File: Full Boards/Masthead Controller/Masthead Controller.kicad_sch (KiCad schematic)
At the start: 181 parts, among them Q1 2N7002, Q2 2N7002, Q3 BSS138P,215, Q4 BSS138P,215, SW1 SW_MEC_5G, SW2 SW_MEC_5G

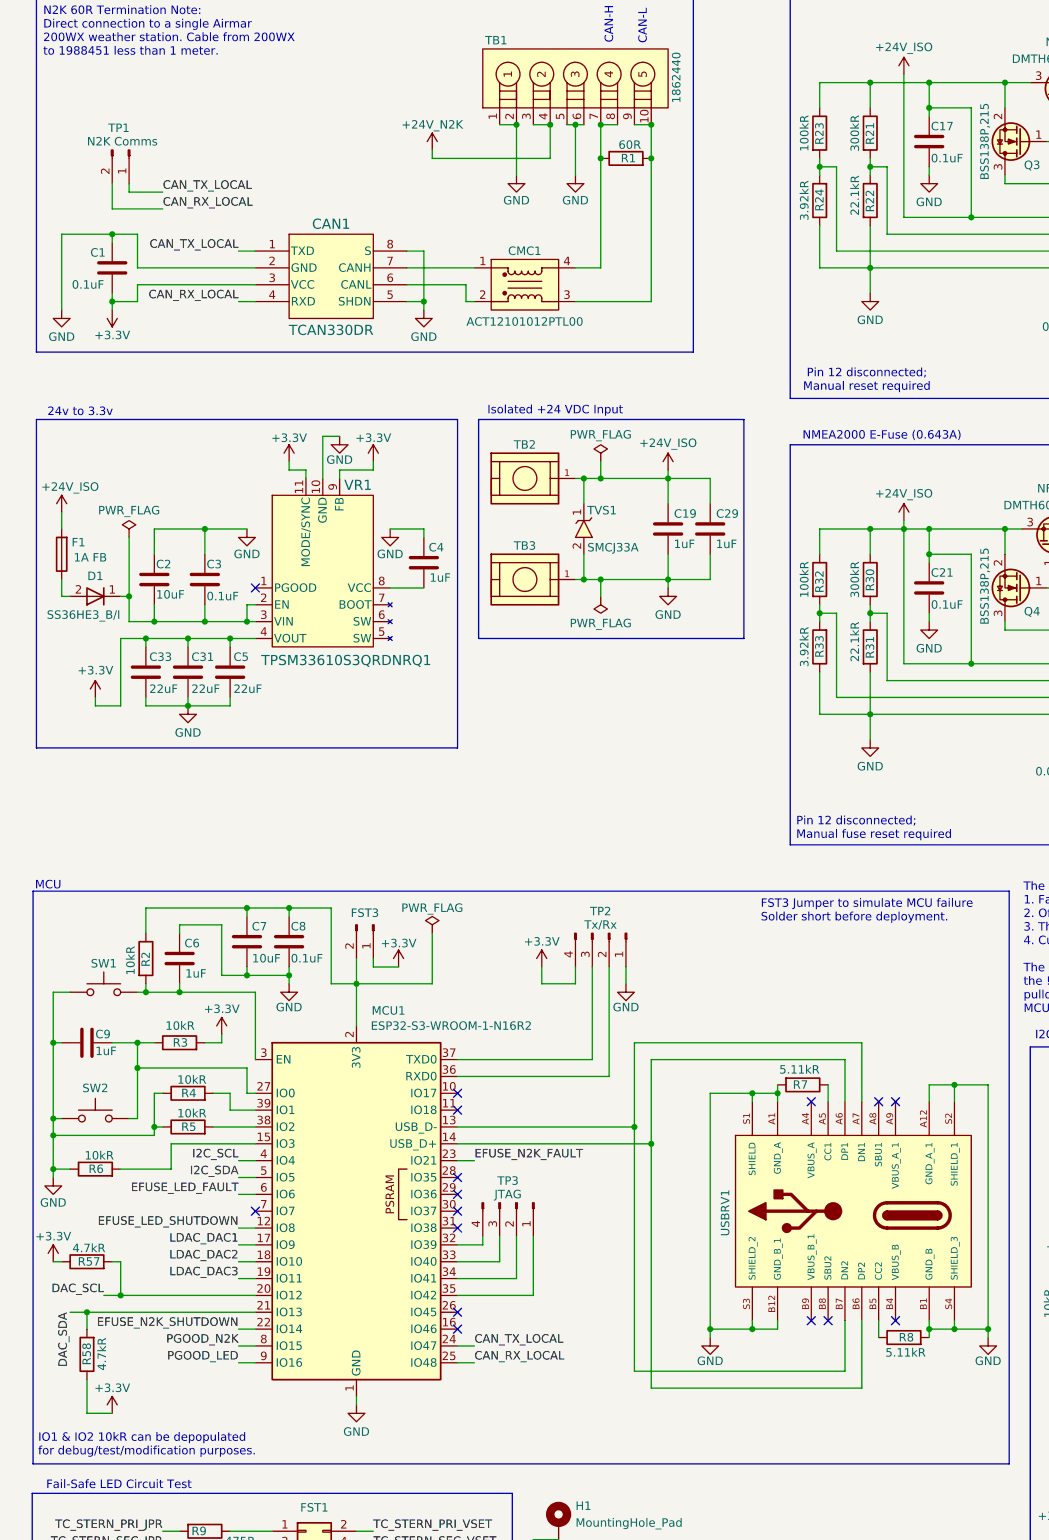
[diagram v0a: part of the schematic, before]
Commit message: Beginning work to enable powering the MCU over USB.
Signed-off-by: digimer <digital.mermaid@gmail.com>
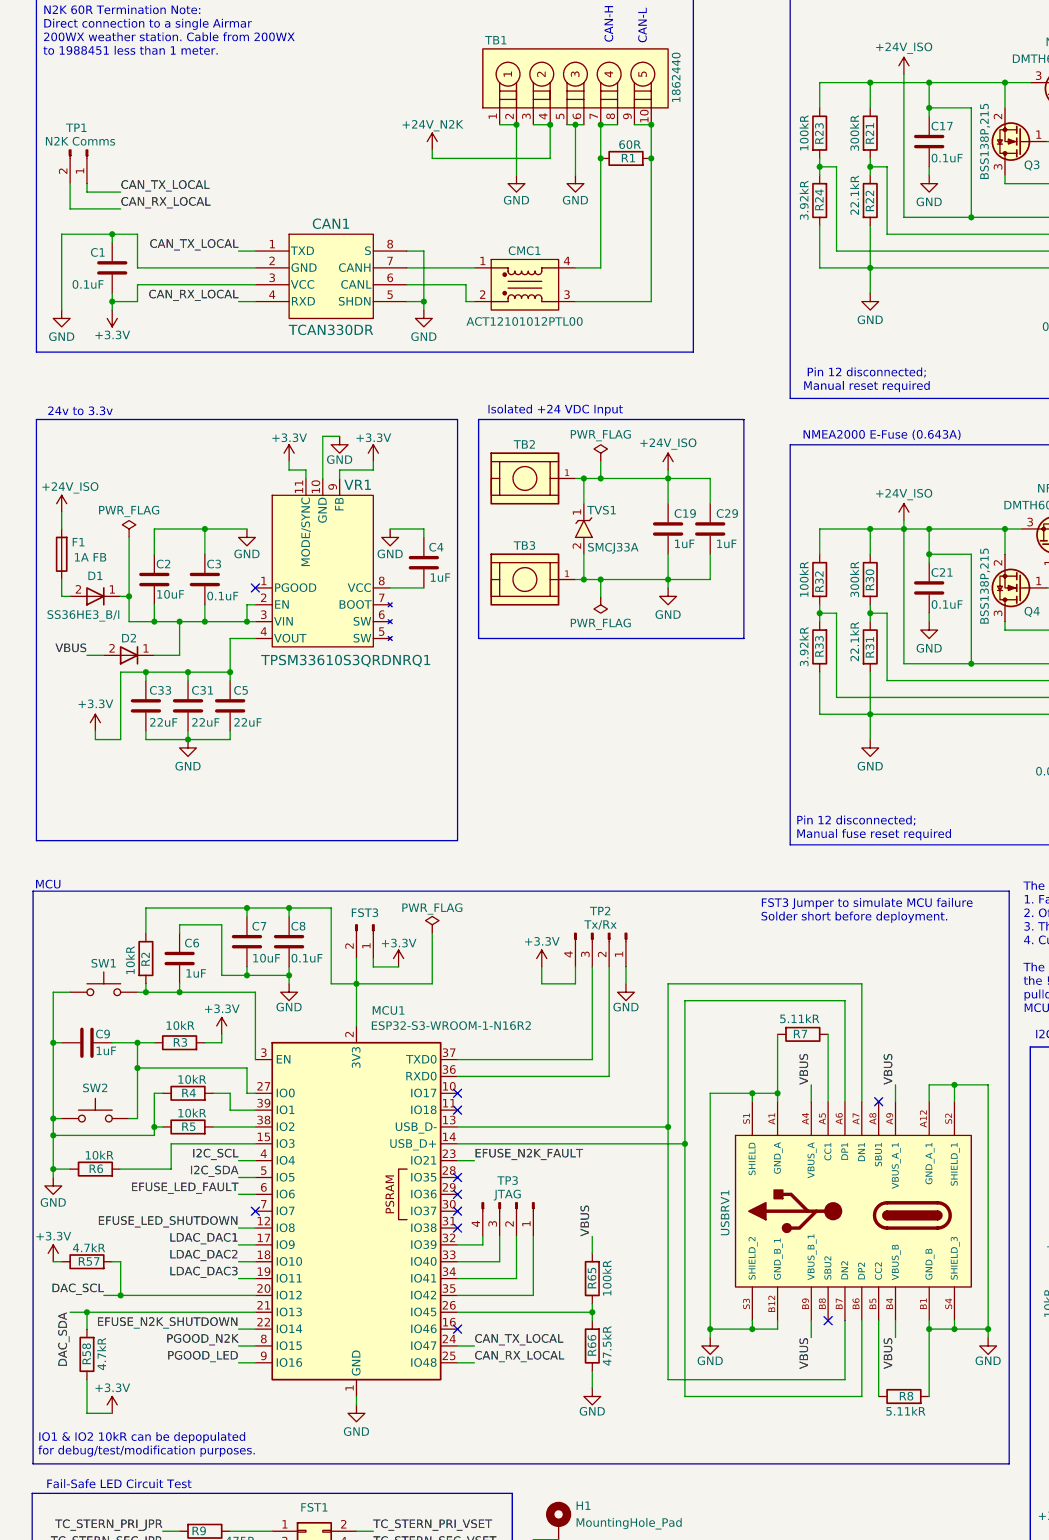
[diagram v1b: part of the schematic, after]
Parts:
- added D2: (no value), mr-stuff:Vishay SS36HE3_BI, symbol mr-parts:Vishay_SS36HE3_B/I
- added R65: 100kR, mr-stuff:Stackpole_RNCP1206, symbol Device:R
- added R66: 47.5kR, mr-stuff:Stackpole_RNCP1206, symbol Device:R
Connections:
- net GND: now also R66.1
- net at C2.2, C3.2, D1.1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: now also D2.1
- net VBUS: now reaches USBRV1.A4 (VBUS_A)
- net VBUS: now also USBRV1.A9 (VBUS_A_1), USBRV1.B4 (VBUS_B), USBRV1.B9 (VBUS_B_1), D2.2, R65.2
- net at MCU1.26 (IO45): now also R65.1, R66.2
- no-connect marks 18 -> 13
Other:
- moved on the sheet: C31, C33, C5, R7, R8, TP1

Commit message: Corrected implementation
Signed-off-by: digimer <digital.mermaid@gmail.com>
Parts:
- D2: value (none) -> SS36HE3_B/I; Part (none) -> Vishay SS36HE3_B/I
- R66: value 47.5kR -> 15kR; Part Stackpole RNCP1206FTD47K5 -> Stackpole RNCP1206FTD15K0
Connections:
- net VBUS_MCU: now reaches R65.1, R66.2
- net VBUS_MCU: now also MCU1.7 (IO7); no longer MCU1.26 (IO45)
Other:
- moved on the sheet: C31, C33, C5, R65, R66

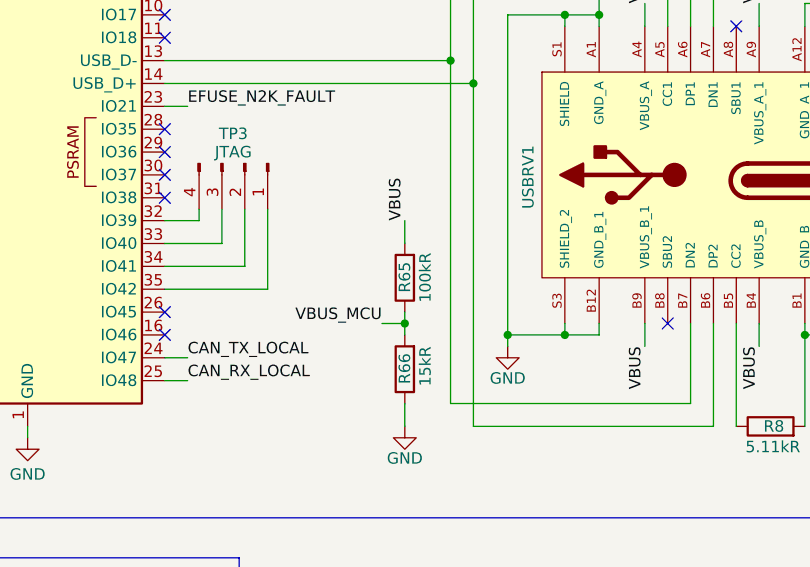
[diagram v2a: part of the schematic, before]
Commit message: Fixed divider resistor value.
Signed-off-by: digimer <digital.mermaid@gmail.com>
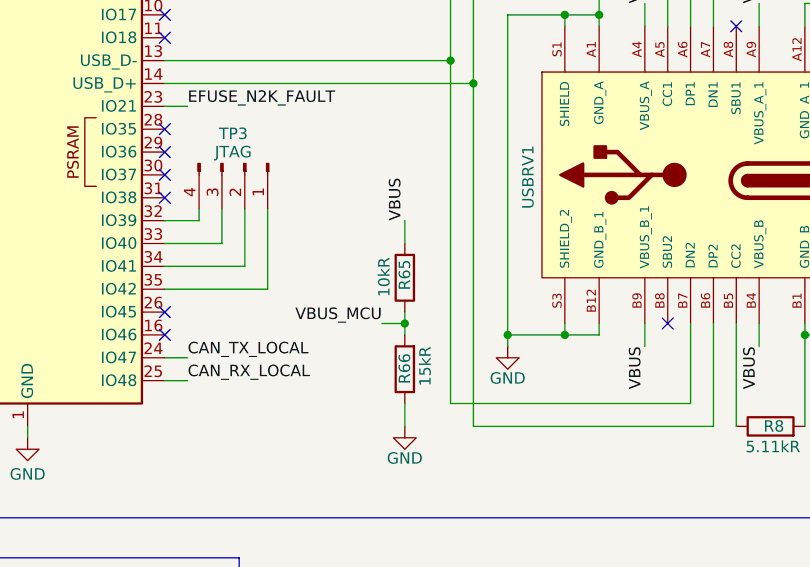
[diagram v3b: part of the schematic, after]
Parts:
- R65: value 100kR -> 10kR
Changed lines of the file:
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@@
 	)
 	(symbol
-		(lib_id "Device:R")
-		(at 105.41 210.82 180)
-		(unit 1)
-		(body_style 1)
-		(exclude_from_sim no)
-		(in_bom yes)
-		(on_board yes)
-		(in_pos_files yes)
-		(dnp no)
-		(property "Reference" "R65"
-			(at 105.41 209.042 90)
-			(show_name no)
-			(do_not_autoplace no)
-			(effects
-				(font
-					(size 1.27 1.27)
-				)
-				(justify left)
-			)
-		)
-		(property "Value" "100kR"
-			(at 107.696 208.026 90)
-			(show_name no)
-			(do_not_autoplace no)
-			(effects
-				(font
-					(size 1.27 1.27)
-				)
-				(justify left)
-			)
-		)
-		(property "Footprint" "mr-stuff:Stackpole_RNCP1206"
-			(at 107.188 210.82 90)
-			(hide yes)
-			(show_name no)
-			(do_not_autoplace no)
-			(effects
-				(font
-					(size 1.27 1.27)
-				)
-			)
-		)
-		(property "Datasheet" ""
-			(at 105.41 210.82 0)
-			(hide yes)
-			(show_name no)
-			(do_not_autoplace no)
-			(effects
-				(font
-					(size 1.27 1.27)
-				)
-			)
-		)
-		(property "Description" "Resistor"
-			(at 105.41 210.82 0)
-			(hide yes)
-			(show_name no)
-			(do_not_autoplace no)
-			(effects
-				(font
-					(size 1.27 1.27)
-				)
-			)
-		)
-		(pin "2"
-		)
-		(pin "1"
-		)
-		(instances
-			(project "Masthead Controller"
-				(path "/2a070473-cb6e-4844-8f2a-5ea6a35ddb49"
-					(reference "R65")
-					(unit 1)
-				)
-			)
-		)
-	)
-	(symbol
 		(lib_id "power:PWR_FLAG")
 		(at 29.21 97.79 0)
@@
 					(unit 1)
 				)
+			)
+		)
+	)
+	(symbol
+		(lib_id "Device:R")
+		(at 105.41 210.82 180)
+		(unit 1)
+		(body_style 1)
+		(exclude_from_sim no)
+		(in_bom yes)
+		(on_board yes)
+		(in_pos_files yes)
+		(dnp no)
+		(property "Reference" "R65"
+			(at 105.41 208.788 90)
+			(show_name no)
+			(do_not_autoplace no)
+			(effects
+				(font
+					(size 1.27 1.27)
+				)
+				(justify left)
+			)
+		)
+		(property "Value" "10kR"
+			(at 103.124 208.534 90)
+			(show_name no)
+			(do_not_autoplace no)
+			(effects
+				(font
+					(size 1.27 1.27)
+				)
+				(justify left)
+			)
+		)
+		(property "Footprint" "mr-stuff:Stackpole_RNCP1206"
+			(at 107.188 210.82 90)
+			(hide yes)
+			(show_name no)
+			(do_not_autoplace no)
+			(effects
+				(font
+					(size 1.27 1.27)
+				)
+			)
+		)
+		(property "Datasheet" ""
+			(at 105.41 210.82 0)
+			(hide yes)
+			(show_name no)
+			(do_not_autoplace no)
+			(effects
+				(font
+					(size 1.27 1.27)
+				)
+			)
+		)
+		(property "Description" "Resistor"
+			(at 105.41 210.82 0)
+			(hide yes)
+			(show_name no)
+			(do_not_autoplace no)
+			(effects
+				(font
+					(size 1.27 1.27)
+				)
+			)
+		)
+		(pin "2"
+		)
+		(pin "1"
+		)
+		(instances
+			(project "Masthead Controller"
+				(path "/2a070473-cb6e-4844-8f2a-5ea6a35ddb49"
+					(reference "R65")
+					(unit 1)
+				)

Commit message: Implemented the changes needed to power the MCU from USB.
Signed-off-by: digimer <digital.mermaid@gmail.com>
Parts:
- D2: value SS36HE3_B/I -> ZLLS500QTA; footprint mr-stuff:Vishay SS36HE3_BI -> Package_TO_SOT_SMD:SOT-23-3; Part Vishay SS36HE3_B/I -> Diodes Inc ZLLS500QTA
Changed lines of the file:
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@@
 	)
 	(junction
+		(at 105.41 205.74)
+		(diameter 0)
+		(color 0 0 0 0)
+	)
+	(junction
 		(at 501.65 119.38)
 		(diameter 0)
@@
 	(wire
 		(pts
+			(xy 105.41 205.74) (xy 105.41 207.01)
+		)
+		(stroke
+			(width 0)
+			(type default)
+		)
+	)
+	(wire
+		(pts
 			(xy 168.91 114.3) (xy 177.8 114.3)
 		)
@@
 	(wire
 		(pts
+			(xy 100.33 205.74) (xy 105.41 205.74)
+		)
+		(stroke
+			(width 0)
+			(type default)
+		)
+	)
+	(wire
+		(pts
 			(xy 45.72 201.93) (xy 48.26 201.93)
 		)
@@
 	(wire
 		(pts
+			(xy 100.33 200.66) (xy 100.33 205.74)
+		)
+		(stroke
+			(width 0)
+			(type default)
+		)
+	)
+	(wire
+		(pts
 			(xy 265.43 40.64) (xy 267.97 40.64)
 		)
@@
 	(wire
 		(pts
-			(xy 105.41 204.47) (xy 105.41 207.01)
+			(xy 105.41 204.47) (xy 105.41 205.74)
 		)
 		(stroke
@@
 			)
 		)
-		(property "Value" "SS36HE3_B/I"
+		(property "Value" "ZLLS500QTA"
 			(at 29.21 118.11 0)
 			(show_name no)
@@
 			)
 		)
-		(property "Footprint" "mr-stuff:Vishay SS36HE3_BI"
+		(property "Footprint" "Package_TO_SOT_SMD:SOT-23-3"
 			(at 29.21 104.394 0)
 			(hide yes)
@@
 			)
 		)
-		(property "Datasheet" "https://www.vishay.com/docs/88751/ss32.pdf"
+		(property "Datasheet" "https://www.diodes.com/assets/Datasheets/ZLLS500QTA.pdf"
 			(at 29.21 102.362 0)
 			(hide yes)
@@
 			)
 		)
-		(property "Description" "Diode 60 V 3A Surface Mount DO-214AB (SMC)"
+		(property "Description" "Diode 40 V 700mA Surface Mount SOT-23-3"
 			(at 29.21 106.68 0)
 			(hide yes)
@@
 			)
 		)
-		(property "Part" "Vishay SS36HE3_B/I"
+		(property "Part" "Diodes Inc ZLLS500QTA"
 			(at 29.21 115.57 0)
 			(hide yes)
@@
 	)
 	(symbol
+		(lib_id "power:PWR_FLAG")
+		(at 100.33 200.66 0)
+		(unit 1)
+		(body_style 1)
+		(exclude_from_sim no)
+		(in_bom yes)
+		(on_board yes)
+		(in_pos_files yes)
+		(dnp no)
+		(property "Reference" "#FLG0110"
+			(at 100.33 198.755 0)
+			(hide yes)
+			(show_name no)
+			(do_not_autoplace no)
+			(effects
+				(font
+					(size 1.27 1.27)
+				)
+			)
+		)
+		(property "Value" "PWR_FLAG"
+			(at 100.33 196.596 0)
+			(show_name no)
+			(do_not_autoplace no)
+			(effects
+				(font
+					(size 1.27 1.27)
+				)
+			)
+		)
+		(property "Footprint" ""
+			(at 100.33 200.66 0)
+			(hide yes)
+			(show_name no)
+			(do_not_autoplace no)
+			(effects
+				(font
+					(size 1.27 1.27)
+				)
+			)
+		)
+		(property "Datasheet" ""
+			(at 100.33 200.66 0)
+			(hide yes)
+			(show_name no)
+			(do_not_autoplace no)
+			(effects
+				(font
+					(size 1.27 1.27)
+				)
+			)
+		)
+		(property "Description" "Special symbol for telling ERC where power comes from"
+			(at 100.33 200.66 0)
+			(hide yes)
+			(show_name no)
+			(do_not_autoplace no)
+			(effects
+				(font
+					(size 1.27 1.27)
+				)
+			)
+		)
+		(pin "1"
+		)
+		(instances
+			(project "Masthead Controller"
+				(path "/2a070473-cb6e-4844-8f2a-5ea6a35ddb49"
+					(reference "#FLG0110")
+					(unit 1)
+				)
+			)
+		)
+	)
+	(symbol
 		(lib_id "power:GND")
 		(at 90.17 276.86 0)
@@
 		)
 		(property "Value" "10kR"
-			(at 103.124 208.534 90)
+			(at 107.696 208.534 90)
 			(show_name no)
 			(do_not_autoplace no)

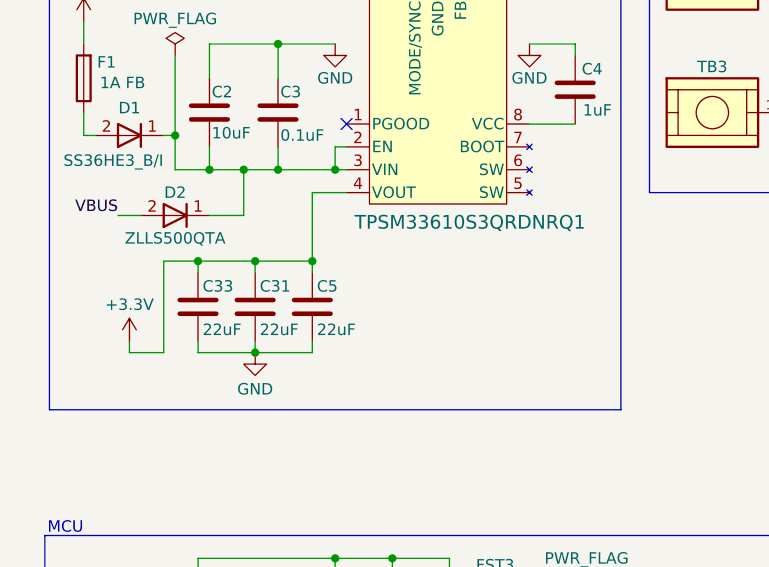
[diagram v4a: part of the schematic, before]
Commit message: Created a symbol and footprint specifically for ZLLS500, and corrected both the schematic and footprint to match.
Signed-off-by: digimer <digital.mermaid@gmail.com>
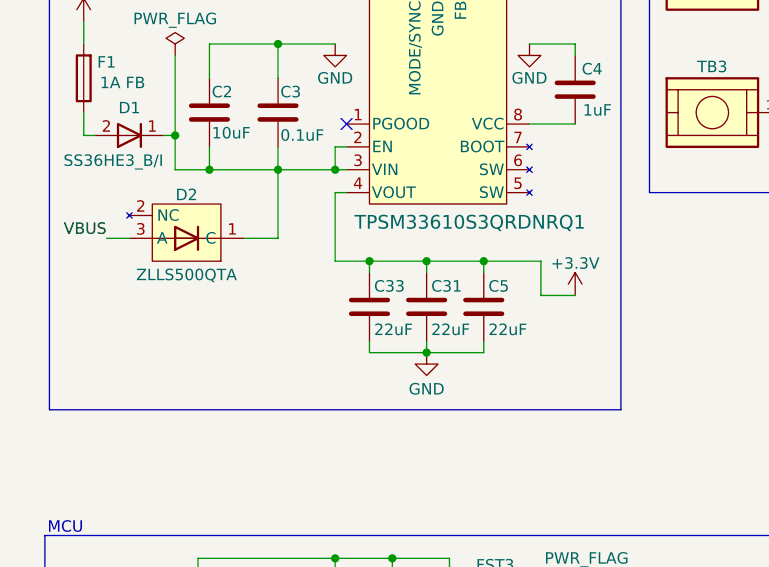
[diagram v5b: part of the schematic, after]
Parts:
- D2: footprint Package_TO_SOT_SMD:SOT-23-3 -> mr-stuff:Diodes Inc ZLLS500; symbol mr-parts:Vishay_SS36HE3_B/I -> mr-parts:Diodes Inc ZLLS500QTA
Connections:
- net VBUS: now also D2.3 (A); no longer D2.2
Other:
- moved on the sheet: C31, C33, C5

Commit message: Fixed the metadata for C11 to properly ID is as a Kemet part. Created a dedicated footprint for that family of caps.
Signed-off-by: digimer <digital.mermaid@gmail.com>
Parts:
- C11: footprint mr-stuff:Kyocera AVX 1206 -> mr-stuff:Kemet C1206C
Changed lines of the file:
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@@
 			)
 		)
-		(property "Footprint" "mr-stuff:Kyocera AVX 1206"
+		(property "Footprint" "mr-stuff:Kemet C1206C"
 			(at 174.9552 67.31 0)
 			(hide yes)

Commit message: Actually fixed Kyocera/Kemet metadata mistake this time.
Signed-off-by: digimer <digital.mermaid@gmail.com>
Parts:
- C11: Part Kyocera C1206C103K1RACAUTO -> Kemet C1206C103K1RACAUTO
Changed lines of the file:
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@@
 			)
 		)
-		(property "Part" "Kyocera C1206C103K1RACAUTO"
+		(property "Part" "Kemet C1206C103K1RACAUTO"
 			(at 173.99 63.5 0)
 			(hide yes)

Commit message: Fixed name for C13 as well.
Signed-off-by: digimer <digital.mermaid@gmail.com>
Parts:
- C13: footprint mr-stuff:Kyocera AVX 1206 -> mr-stuff:Kemet C1206C; Part Kyocera C1206X473K1RACAUTO -> Kemet C1206X473K1RACAUTO
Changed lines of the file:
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@@
 			)
 		)
-		(property "Footprint" "mr-stuff:Kyocera AVX 1206"
+		(property "Footprint" "mr-stuff:Kemet C1206C"
 			(at 174.9552 134.62 0)
 			(hide yes)
@@
 			)
 		)
-		(property "Part" "Kyocera C1206X473K1RACAUTO"
+		(property "Part" "Kemet C1206X473K1RACAUTO"
 			(at 173.99 130.81 0)
 			(hide yes)
